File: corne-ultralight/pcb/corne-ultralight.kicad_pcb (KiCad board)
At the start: 2 copper layers, 275.5 x 105.6 mm, 126 parts, among them J2 OLED, J5 Breakaway_Tabs, J7 OLED, SW1 SW_PUSH, SW10 SW_PUSH, SW11 SW_PUSH, SW12 SW_PUSH, SW13 SW_PUSH, SW14 SW_PUSH, SW15 SW_PUSH, SW16 SW_PUSH, SW17 SW_PUSH, SW18 SW_PUSH, SW19 SW_PUSH, SW2 SW_PUSH, SW20 SW_PUSH, SW21 SW_PUSH, SW22 SW_PUSH, SW23 SW_PUSH, SW24 SW_PUSH, SW25 SW_PUSH, SW26 SW_PUSH, SW27 SW_PUSH, SW28 SW_PUSH, SW29 SW_PUSH, SW3 SW_PUSH, SW30 SW_PUSH, SW31 SW_PUSH, SW32 SW_PUSH, SW33 SW_PUSH, SW34 SW_PUSH, SW35 SW_PUSH, SW36 SW_PUSH, SW37 SW_PUSH, SW38 SW_PUSH, SW39 SW_PUSH, SW4 SW_PUSH, SW40 SW_PUSH, SW41 SW_PUSH, SW42 SW_PUSH, SW5 SW_PUSH, SW6 SW_PUSH, SW7 SW_PUSH, SW8 SW_PUSH, SW9 SW_PUSH, U1 ProMicro, U2 ProMicro

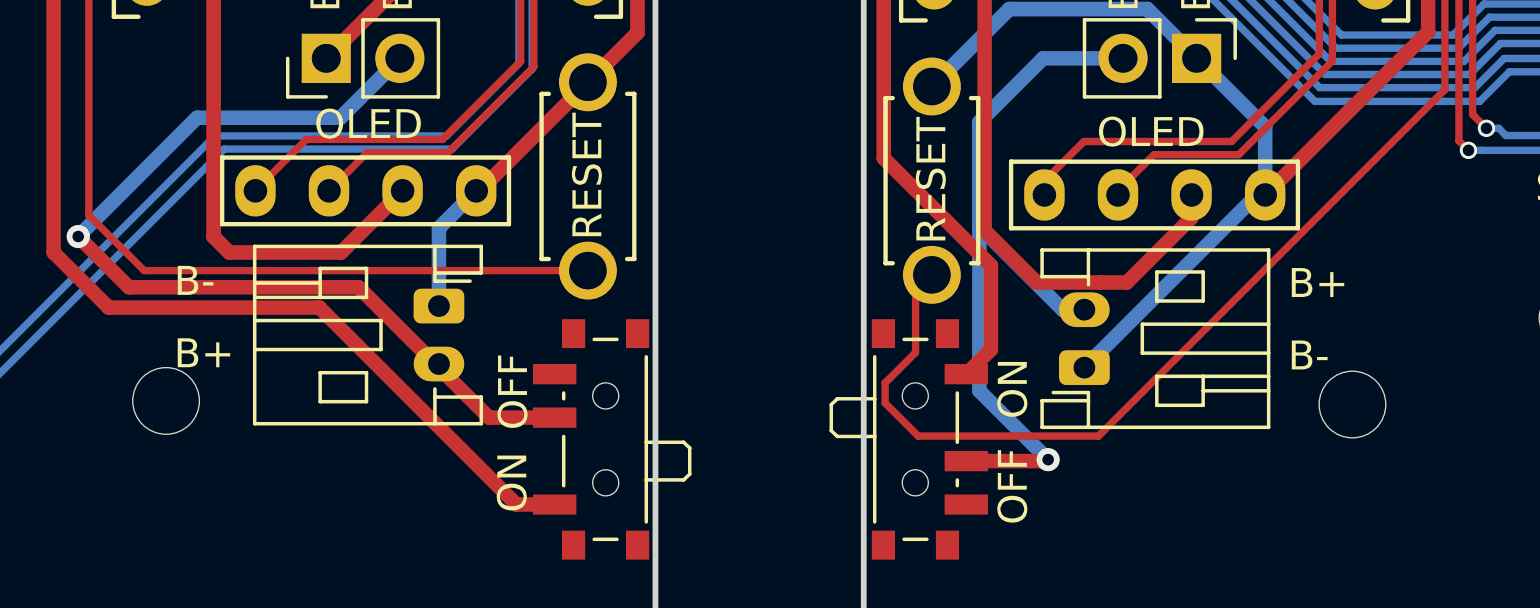
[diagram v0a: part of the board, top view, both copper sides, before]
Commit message: Adjust JST polarity.
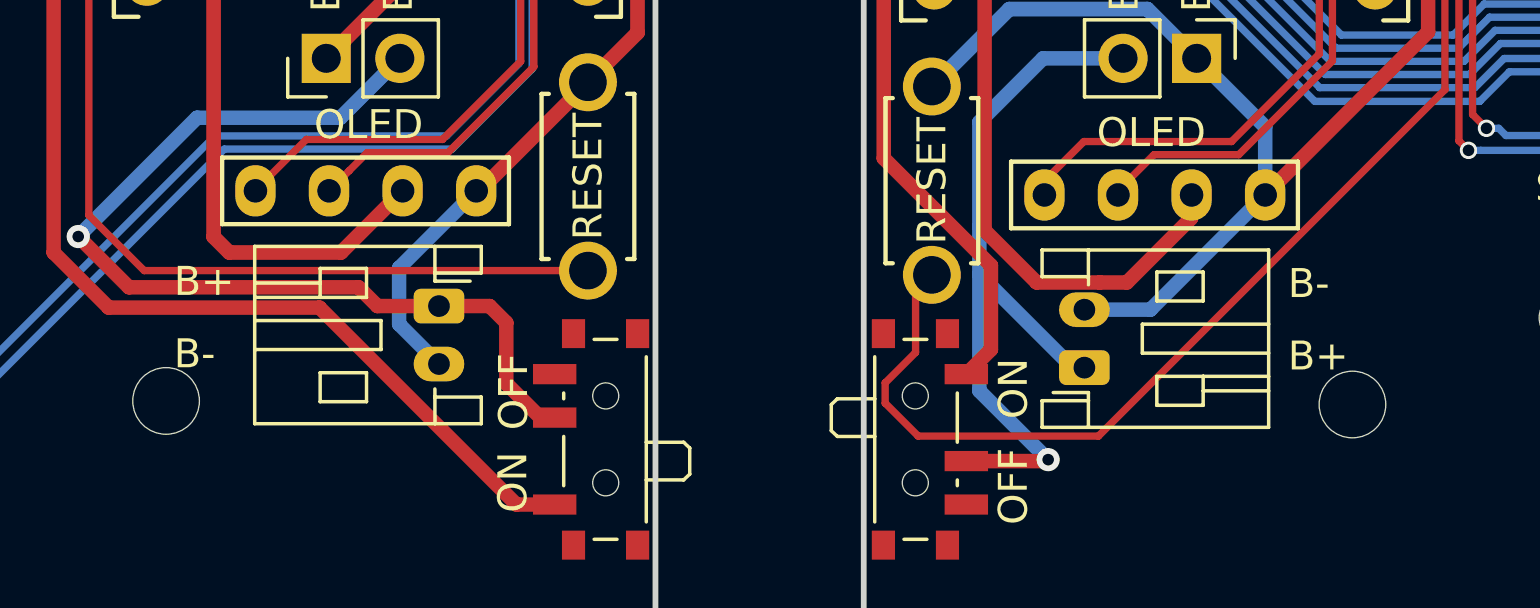
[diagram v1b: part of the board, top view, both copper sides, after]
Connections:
- BATJ2 pad 1: GND -> Net-(BATJ1-Pad2)
- BATJ2 pad 2: Net-(BATJ1-Pad2) -> GND
- BATJ4 pad 1: GNDA -> Net-(BATJ3-Pad2)
- BATJ4 pad 2: Net-(BATJ3-Pad2) -> GNDA
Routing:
- net GND: track 80.5 -> 83.6 mm
- net Net-(BATJ1-Pad2): track 32.7 -> 33.9 mm
- net GNDA: track 74.7 -> 73.9 mm

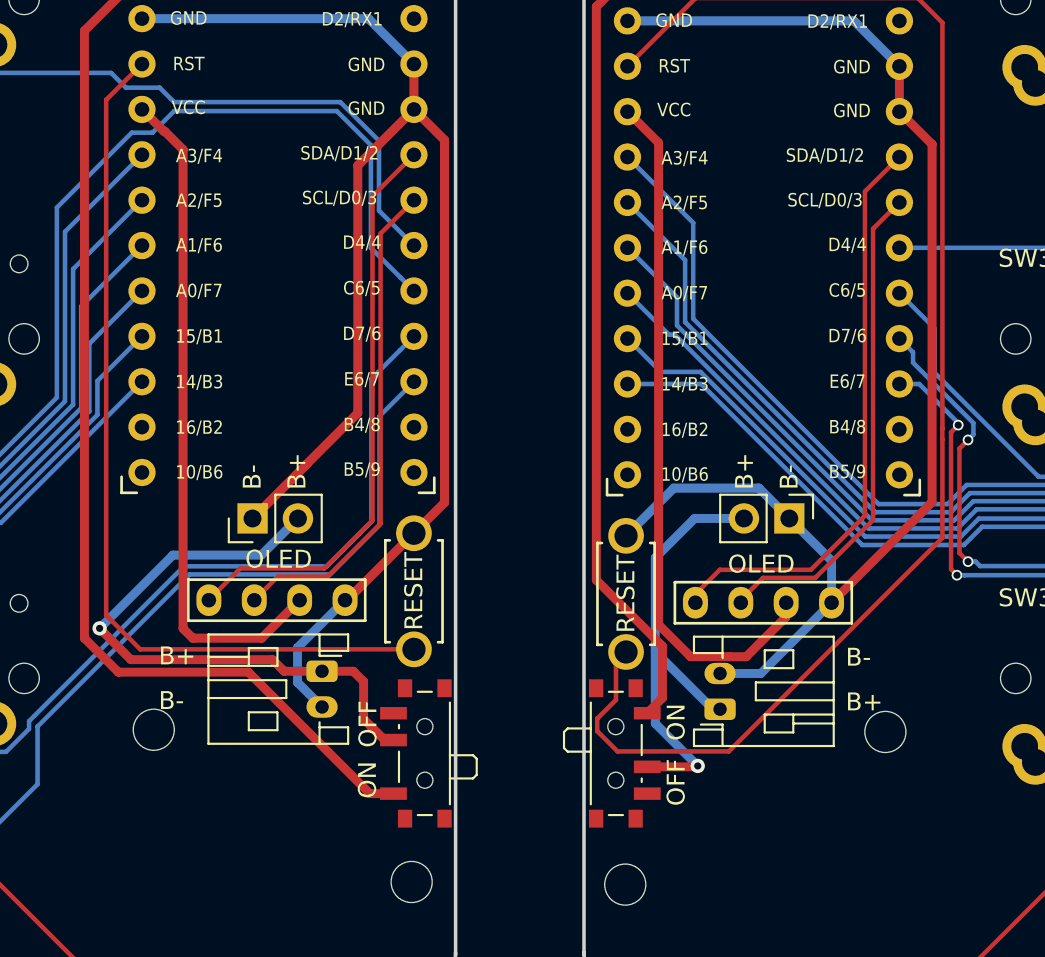
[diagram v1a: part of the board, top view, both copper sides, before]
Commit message: More silk/JST fixes.
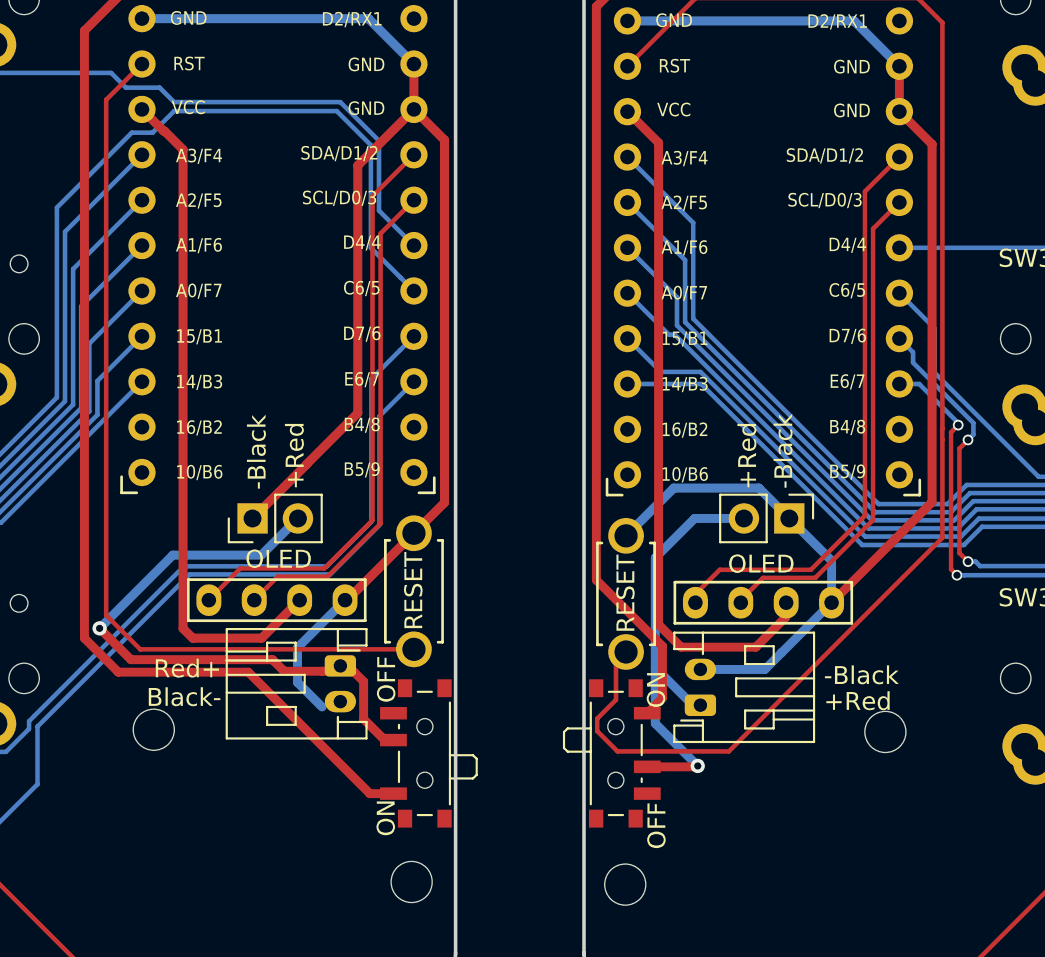
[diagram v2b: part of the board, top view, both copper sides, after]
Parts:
- moved BATJ4 1.12 mm to (160.5, 83.0)
- moved BATJ2 1.07 mm to (140.4, 80.8)
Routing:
- net Net-(BATJ3-Pad2): track 26.3 -> 24.7 mm
- net GNDA: track 73.9 -> 74.9 mm
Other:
- board text added: "+Red"
- board text added: "-Black"
- board text added: "Black-"
- board text added: "Red+"
- board text removed: "B+"
- board text removed: "B-"
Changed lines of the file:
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@@
   )
   (footprint "Connector_JST:JST_PH_S2B-PH-K_1x02_P2.00mm_Horizontal" (layer "F.Cu")
-    (at 161.6375 83.27 90)
+    (at 160.5375 83.045 90)
     (descr "JST PH series connector, S2B-PH-K (http://www.jst-mfg.com/product/pdf/eng/ePH.pdf), generated with kicad-footprint-generator")
     (tags "connector JST PH top entry")
@@
     (pad "2" thru_hole oval (at 0 2.54 270) (size 1.7 1.7) (drill 1) (layers *.Cu *.Mask)
       (net 88 "Net-(BATJ3-Pad2)") (pinfunction "Pin_2") (pintype "passive"))
-    (model "${KICAD6_3DMODEL_DIR}/Connector_PinHeader_2.54mm.3dshapes/PinHeader_1x02_P2.54mm_Vertical.wrl"
-      (offset (xyz 0 0 0))
-      (scale (xyz 1 1 1))
-      (rotate (xyz 0 0 0))
-    )
   )
   (footprint "Connector_PinHeader_2.54mm:PinHeader_1x02_P2.54mm_Vertical" (layer "F.Cu")
@@
     (pad "2" thru_hole oval (at 0 2.54 90) (size 1.7 1.7) (drill 1) (layers *.Cu *.Mask)
       (net 37 "Net-(BATJ1-Pad2)") (pinfunction "Pin_2") (pintype "passive"))
-    (model "${KICAD6_3DMODEL_DIR}/Connector_PinHeader_2.54mm.3dshapes/PinHeader_1x02_P2.54mm_Vertical.wrl"
-      (offset (xyz 0 0 0))
-      (scale (xyz 1 1 1))
-      (rotate (xyz 0 0 0))
-    )
   )
   (footprint "Button_Switch_SMD:SW_SPDT_PCM12" (layer "F.Cu")
@@
   )
   (footprint "Connector_JST:JST_PH_S2B-PH-K_1x02_P2.00mm_Horizontal" (layer "F.Cu")
-    (at 139.3625 81.145 -90)
+    (at 140.3875 80.845 -90)
     (descr "JST PH series connector, S2B-PH-K (http://www.jst-mfg.com/product/pdf/eng/ePH.pdf), generated with kicad-footprint-generator")
     (tags "connector JST PH top entry")
@@
     (effects (font (size 1 1) (thickness 0.125)) (justify left))
   )
-  (gr_text "B-" (at 168.6625 80.37) (layer "F.SilkS")
+  (gr_text "-Black" (at 167.4375 81.395) (layer "F.SilkS")
     (effects (font (size 1 1) (thickness 0.15)) (justify left))
   )
-  (gr_text "OFF" (at 159.1875 88.695 90) (layer "F.SilkS")
+  (gr_text "OFF" (at 158.1125 91.12 90) (layer "F.SilkS")
     (effects (font (size 1 1) (thickness 0.15)) (justify left))
   )
-  (gr_text "B+" (at 137.9625 71 90) (layer "F.SilkS")
+  (gr_text "+Red" (at 137.8625 70.995 90) (layer "F.SilkS")
     (effects (font (size 1 1) (thickness 0.15)) (justify left))
   )
-  (gr_text "B+" (at 163.0125 71 90) (layer "F.SilkS")
+  (gr_text "+Red" (at 163.1875 70.995 90) (layer "F.SilkS")
     (effects (font (size 1 1) (thickness 0.15)) (justify left))
   )
-  (gr_text "B+" (at 130.2125 80.295) (layer "F.SilkS")
-    (effects (font (size 1 1) (thickness 0.15)) (justify left))
+  (gr_text "Red+" (at 133.7375 81.02) (layer "F.SilkS")
+    (effects (font (size 1 1) (thickness 0.15)) (justify right))
   )
-  (gr_text "B+" (at 168.6625 82.87) (layer "F.SilkS")
+  (gr_text "+Red" (at 167.4375 82.845) (layer "F.SilkS")
     (effects (font (size 1 1) (thickness 0.15)) (justify left))
   )
-  (gr_text "B-" (at 165.5125 71 90) (layer "F.SilkS")
+  (gr_text "-Black" (at 165.2125 70.945 90) (layer "F.SilkS")
     (effects (font (size 1 1) (thickness 0.15)) (justify left))
   )
-  (gr_text "ON" (at 141.9125 86.17 90) (layer "F.SilkS")
+  (gr_text "ON" (at 142.9625 88.295 90) (layer "F.SilkS")
     (effects (font (size 1 1) (thickness 0.15)) (justify right))
   )
-  (gr_text "B-" (at 130.2125 82.795) (layer "F.SilkS")
-    (effects (font (size 1 1) (thickness 0.15)) (justify left))
+  (gr_text "Black-" (at 133.7375 82.62) (layer "F.SilkS")
+    (effects (font (size 1 1) (thickness 0.15)) (justify right))
   )
-  (gr_text "ON" (at 159.1875 85.045 90) (layer "F.SilkS")
+  (gr_text "ON" (at 158.0875 83.22 90) (layer "F.SilkS")
     (effects (font (size 1 1) (thickness 0.15)) (justify left))
   )
-  (gr_text "B-" (at 135.4625 71 90) (layer "F.SilkS")
+  (gr_text "-Black" (at 135.7375 70.995 90) (layer "F.SilkS")
     (effects (font (size 1 1) (thickness 0.15)) (justify left))
   )
-  (gr_text "OFF" (at 141.9375 82.77 90) (layer "F.SilkS")
+  (gr_text "OFF" (at 142.9875 80.27 90) (layer "F.SilkS")
     (effects (font (size 1 1) (thickness 0.15)) (justify right))
   )
@@
   (segment (start 186.395852 73.060432) (end 176.304847 73.060432) (width 0.254) (layer "B.Cu") (net 74))
   (segment (start 186.5625 73.22708) (end 186.395852 73.060432) (width 0.254) (layer "B.Cu") (net 74))
-  (segment (start 163.104847 80.330432) (end 165.314847 78.120432) (width 0.5) (layer "F.Cu") (net 80))
-  (segment (start 158.194847 78.534812) (end 159.990467 80.330432) (width 0.5) (layer "F.Cu") (net 80))
-  (segment (start 165.284847 77.310432) (end 165.189847 77.310432) (width 0.5) (layer "F.Cu") (net 80))
-  (segment (start 156.454247 49.828432) (end 158.194847 51.569032) (width 0.5) (layer "F.Cu") (net 80))
-  (segment (start 162.169847 80.330432) (end 163.104847 80.330432) (width 0.5) (layer "F.Cu") (net 80))
-  (segment (start 158.194847 51.569032) (end 158.194847 78.534812) (width 0.5) (layer "F.Cu") (net 80))
-  (segment (start 159.990467 80.330432) (end 162.169847 80.330432) (width 0.5) (layer "F.Cu") (net 80))
-  (segment (start 165.314847 78.120432) (end 165.314847 77.340432) (width 0.5) (layer "F.Cu") (net 80))
-  (segment (start 165.314847 77.340432) (end 165.284847 77.310432) (width 0.5) (layer "F.Cu") (net 80))
+  (segment (start 163.63889 79.79639) (end 159.456424 79.79639) (width 0.5) (layer "F.Cu") (net 80))
+  (segment (start 158.194847 51.569032) (end 156.454247 49.828432) (width 0.5) (layer "F.Cu") (net 80))
+  (segment (start 158.194847 78.534812) (end 158.194847 51.569032) (width 0.5) (layer "F.Cu") (net 80))
+  (segment (start 165.314847 77.340432) (end 165.314847 78.120432) (width 0.5) (layer "F.Cu") (net 80))
+  (segment (start 165.189847 77.310432) (end 165.284847 77.310432) (width 0.5) (layer "F.Cu") (net 80))
+  (segment (start 159.456424 79.79639) (end 158.194847 78.534812) (width 0.5) (layer "F.Cu") (net 80))
+  (segment (start 165.284847 77.310432) (end 165.314847 77.340432) (width 0.5) (layer "F.Cu") (net 80))
+  (segment (start 165.314847 78.120432) (end 163.63889 79.79639) (width 0.5) (layer "F.Cu") (net 80))
   (segment (start 171.674247 47.288432) (end 171.674247 49.828432) (width 0.5) (layer "F.Cu") (net 81))
   (segment (start 173.501326 51.660333) (end 173.501326 71.686174) (width 0.5) (layer "F.Cu") (net 81))
@@
   (segment (start 171.674247 49.828432) (end 173.503737 51.657922) (width 0.5) (layer "F.Cu") (net 81))
   (segment (start 173.501326 71.686174) (end 167.8775 77.31) (width 0.5) (layer "F.Cu") (net 81))
+  (segment (start 164.1425 81.045) (end 165.0775 80.11) (width 0.5) (layer "B.Cu") (net 81))
   (segment (start 163.8125 70.895) (end 165.5125 72.595) (width 0.508) (layer "B.Cu") (net 81))
   (segment (start 167.8775 77.31) (end 167.8775 74.96) (width 0.5) (layer "B.Cu") (net 81))
-  (segment (start 161.6375 81.27) (end 163.9175 81.27) (width 0.5) (layer "B.Cu") (net 81))
+  (segment (start 160.5375 81.045) (end 164.1425 81.045) (width 0.5) (layer "B.Cu") (net 81))
   (segment (start 159.047279 70.895) (end 163.8125 70.895) (width 0.508) (layer "B.Cu") (net 81))
   (segment (start 156.454247 44.748432) (end 169.134247 44.748432) (width 0.508) (layer "B.Cu") (net 81))
-  (segment (start 163.9175 81.27) (end 167.8775 77.31) (width 0.5) (layer "B.Cu") (net 81))
   (segment (start 169.134247 44.748432) (end 171.674247 47.288432) (width 0.508) (layer "B.Cu") (net 81))
   (segment (start 156.374847 73.567432) (end 159.047279 70.895) (width 0.508) (layer "B.Cu") (net 81))
   (segment (start 167.8775 74.96) (end 165.5125 72.595) (width 0.5) (layer "B.Cu") (net 81))
+  (segment (start 165.0775 80.11) (end 167.8775 77.31) (width 0.5) (layer "B.Cu") (net 81))
   (segment (start 154.7125 43.950179) (end 156.454247 42.208432) (width 0.5) (layer "F.Cu") (net 87))
   (segment (start 158.4125 79.741735) (end 154.7125 76.041735) (width 0.5) (layer "F.Cu") (net 87))
@@
   (segment (start 160.3875 86.445) (end 160.3375 86.495) (width 0.5) (layer "F.Cu") (net 88))
   (via (at 160.3875 86.445) (size 0.8) (drill 0.4) (layers "F.Cu" "B.Cu") (net 88))
+  (segment (start 158.0125 80.945) (end 160.1125 83.045) (width 0.5) (layer "B.Cu") (net 88))
   (segment (start 158.0125 74.795) (end 160.2125 72.595) (width 0.5) (layer "B.Cu") (net 88))
   (segment (start 158.0125 78.395) (end 158.0125 74.795) (width 0.5) (layer "B.Cu") (net 88))
   (segment (start 160.2125 72.595) (end 162.9725 72.595) (width 0.5) (layer "B.Cu") (net 88))
+  (segment (start 158.0125 84.07) (end 158.0125 80.945) (width 0.5) (layer "B.Cu") (net 88))
   (segment (start 160.3875 86.445) (end 158.0125 84.07) (width 0.5) (layer "B.Cu") (net 88))
   (segment (start 158.0125 80.045) (end 158.0125 78.395) (width 0.5) (layer "B.Cu") (net 88))
-  (segment (start 161.2375 83.27) (end 161.6375 83.27) (width 0.5) (layer "B.Cu") (net 88))
-  (segment (start 158.0125 80.045) (end 161.2375 83.27) (width 0.5) (layer "B.Cu") (net 88))
-  (segment (start 158.0125 84.07) (end 158.0125 80.045) (width 0.5) (layer "B.Cu") (net 88))
+  (segment (start 160.1125 83.045) (end 160.5375 83.045) (width 0.5) (layer "B.Cu") (net 88))
+  (segment (start 158.0125 80.945) (end 158.0125 80.045) (width 0.5) (layer "B.Cu") (net 88))
 )

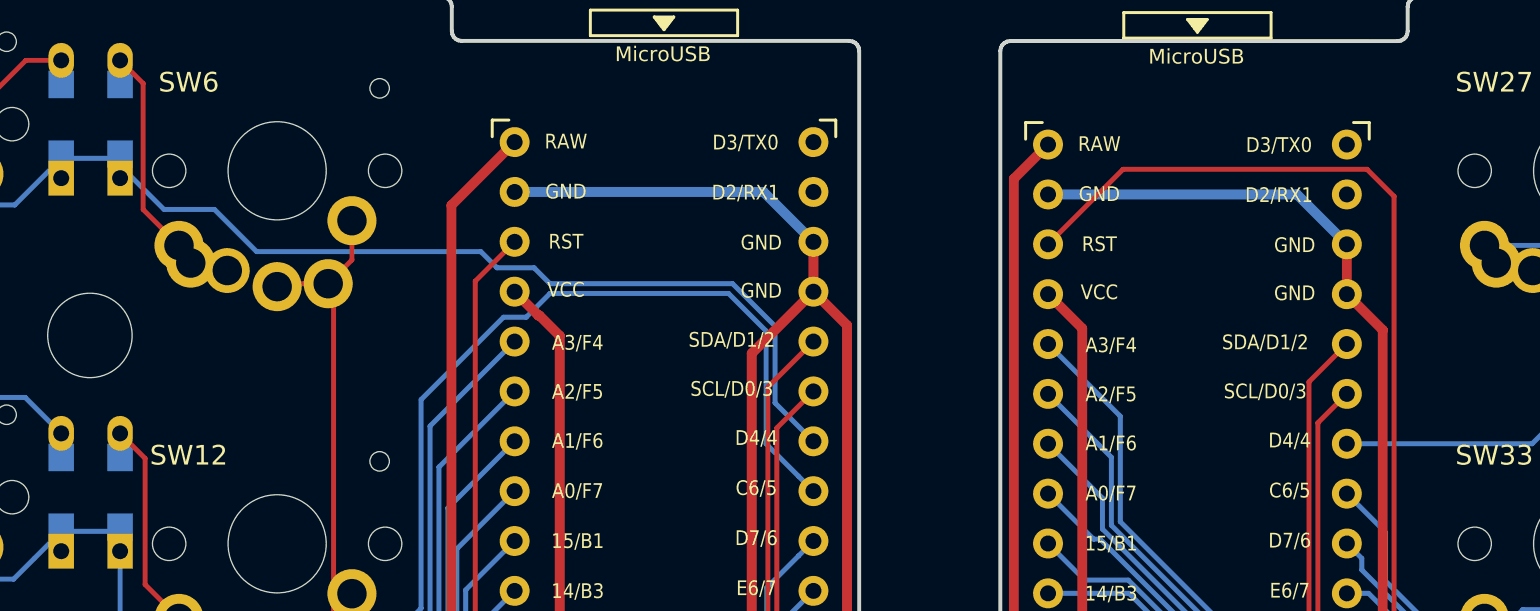
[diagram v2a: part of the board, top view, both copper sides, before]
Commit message: Add test points for RGB strip.
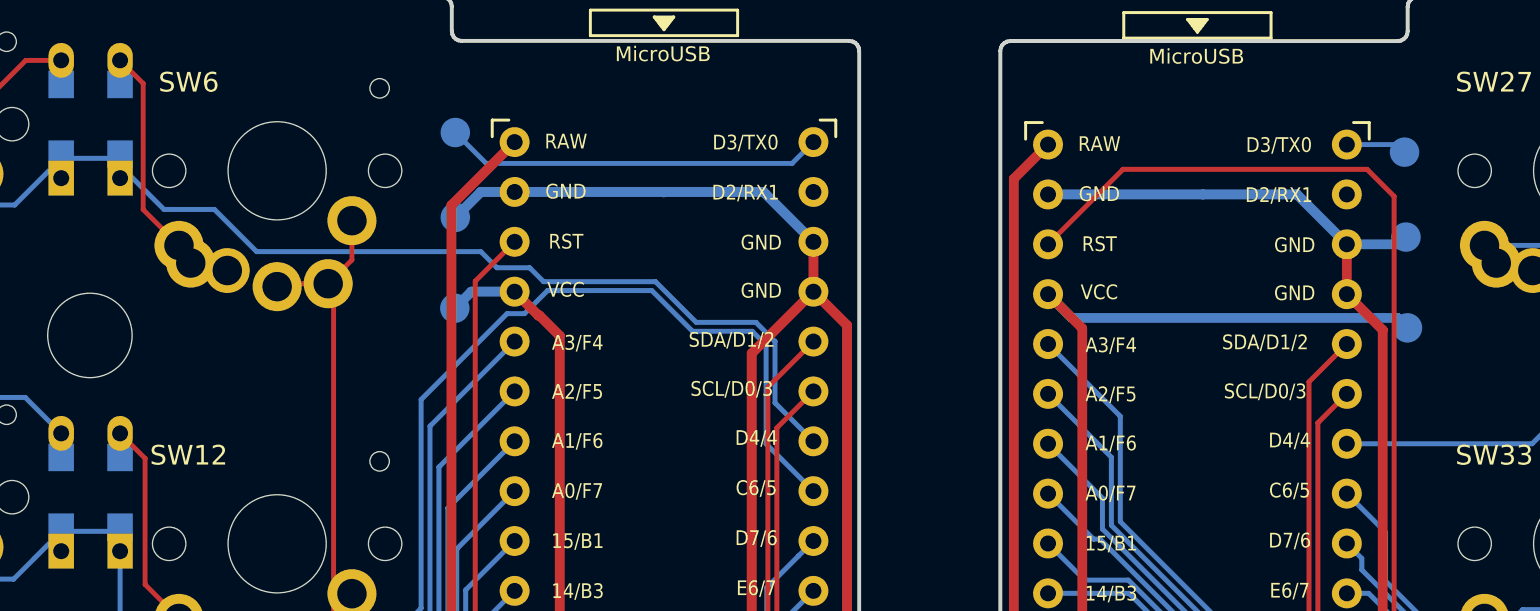
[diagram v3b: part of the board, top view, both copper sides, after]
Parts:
- added TP1: RGB, TestPoint:TestPoint_Pad_D1.5mm, B.Cu at (126.3, 41.6)
- added TP2: VCC, TestPoint:TestPoint_Pad_D1.5mm, B.Cu at (126.2, 50.5)
- added TP3: GND, TestPoint:TestPoint_Pad_D1.5mm, B.Cu at (126.3, 45.9)
- added TP4: RGB, TestPoint:TestPoint_Pad_D1.5mm, B.Cu at (174.6, 42.6)
- added TP5: VCC, TestPoint:TestPoint_Pad_D1.5mm, B.Cu at (174.8, 51.5)
- added TP6: GND, TestPoint:TestPoint_Pad_D1.5mm, B.Cu at (174.7, 46.9)
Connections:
- U1 pad 1: unconnected-(U1-Pad1) -> RGB
- U2 pad 1: unconnected-(U2-Pad1) -> RGB_r
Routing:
- net RGB: track 0.00 -> 19.3 mm
- net VDD: track 38.7 -> 57.7 mm
- net GND: track 83.6 -> 87.2 mm
- net VCC: track 37.7 -> 41.1 mm
- net GNDA: track 74.9 -> 78.1 mm
- net RGB_r: track 0.00 -> 3.10 mm
